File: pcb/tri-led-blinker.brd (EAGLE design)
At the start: 80 x 49 mm, 13 parts, among them J1 MICRO-USB-SMD(ZX62-B-5PA), K1 TS-1109

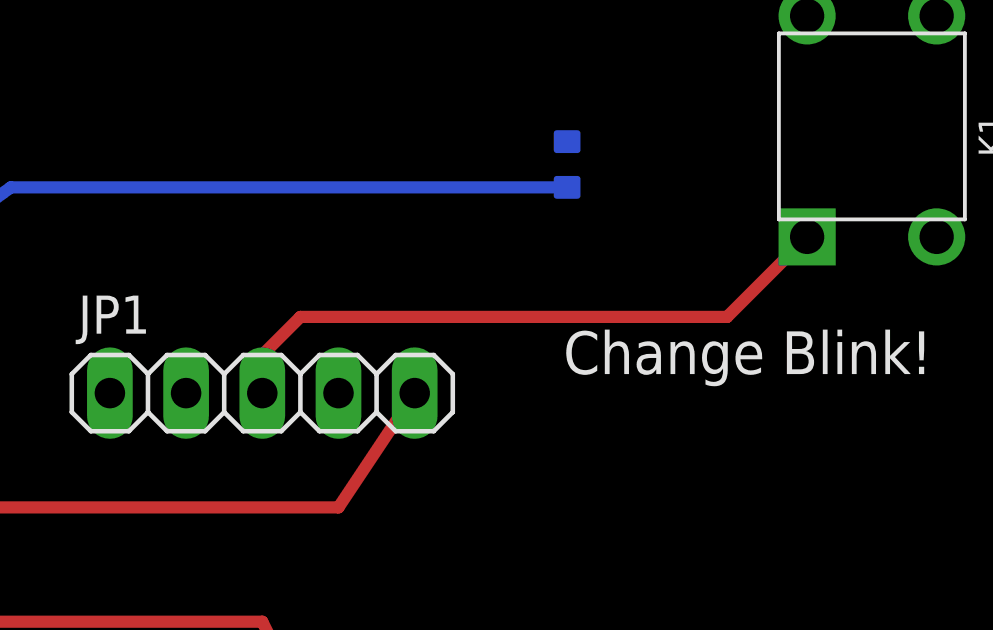
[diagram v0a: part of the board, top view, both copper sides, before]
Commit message: change button input pin to PB3
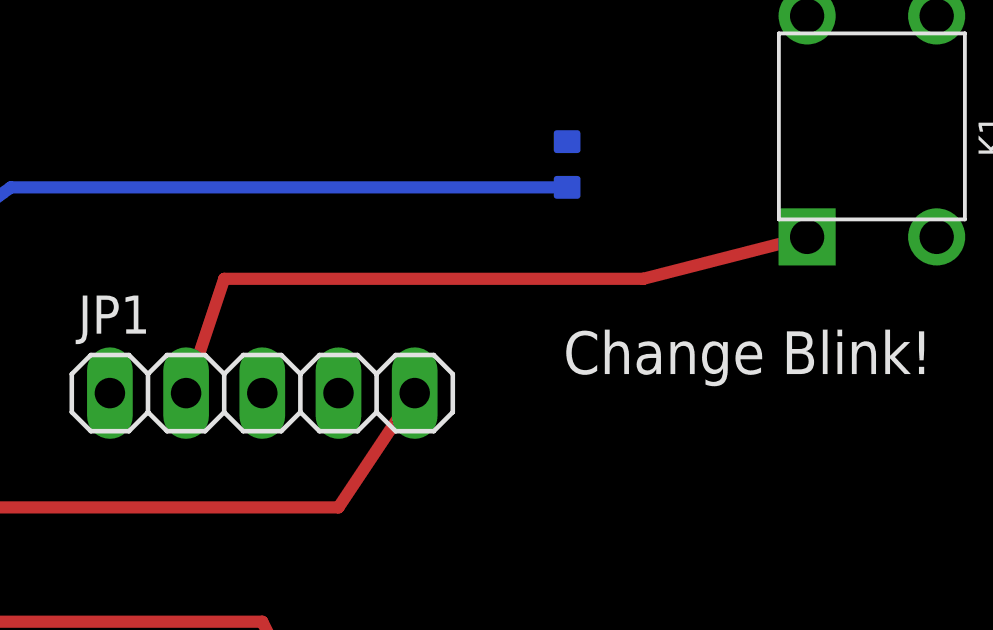
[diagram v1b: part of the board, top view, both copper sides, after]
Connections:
- net N$5: now also JP1.4; no longer JP1.3
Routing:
- net N$5: track 21.1 -> 23.6 mm
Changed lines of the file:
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@@
 <layer number="17" name="Pads" color="2" fill="1" visible="yes" active="yes"/>
 <layer number="18" name="Vias" color="2" fill="1" visible="yes" active="yes"/>
-<layer number="19" name="Unrouted" color="6" fill="1" visible="no" active="yes"/>
+<layer number="19" name="Unrouted" color="6" fill="1" visible="yes" active="yes"/>
 <layer number="20" name="Dimension" color="15" fill="1" visible="yes" active="yes"/>
 <layer number="21" name="tPlace" color="7" fill="1" visible="yes" active="yes"/>
@@
 <signal name="N$5">
 <contactref element="K1" pad="1"/>
-<contactref element="JP1" pad="3"/>
-<wire x1="53.34" y1="31.75" x2="53.34" y2="33.02" width="0.4064" layer="1"/>
-<wire x1="53.34" y1="33.02" x2="54.61" y2="34.29" width="0.4064" layer="1"/>
-<wire x1="54.61" y1="34.29" x2="68.834" y2="34.29" width="0.4064" layer="1"/>
-<wire x1="68.834" y1="34.29" x2="71.501" y2="36.957" width="0.4064" layer="1"/>
+<contactref element="JP1" pad="4"/>
+<wire x1="71.501" y1="36.957" x2="66.04" y2="35.56" width="0.4064" layer="1"/>
+<wire x1="66.04" y1="35.56" x2="52.07" y2="35.56" width="0.4064" layer="1"/>
+<wire x1="52.07" y1="35.56" x2="50.8" y2="31.75" width="0.4064" layer="1"/>
 </signal>
 <signal name="N$8">
